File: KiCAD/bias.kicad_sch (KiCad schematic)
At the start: 52 parts, among them Q2 2N7000, Q3 2N7000, U10 OPA454, U11 LM4040LP-5, U12 LM393, U13 OPA1641, U14 OPA1641, U5 OPA454, U9 LM7805_TO220

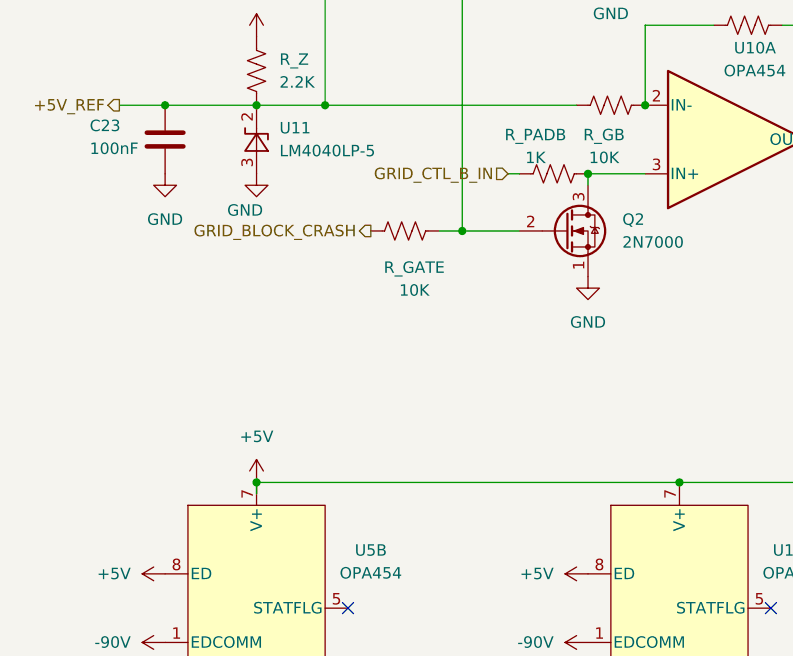
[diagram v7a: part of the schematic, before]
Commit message: front-panel: QT encoder swap, PCF8575 breakout, pre-fab checklist, INT-none decision
Switch STEP + FUNC from direct PCF8575 GPIO to Adafruit I2C QT Rotary
Encoder breakouts (PID 4991) at addr 0x36 / 0x37. The onboard seesaw
SAMD09 handles quadrature decoding + button debounce, dropping ~200
lines of firmware. PCF8575 still covers the LCD (4-bit), paddle, and
panel LEDs.

Add custom KiCad symbols + footprints for both new breakouts to
xmitter.kicad_sym and xmitter.pretty. Footprint properties on the new
symbols are pre-linked, so schematic instances auto-associate. Some
coordinates in both footprints are best-guess pending physical
measurement -- flagged in the descr fields and in the new
front_panel_interface.md open-items subsections.

Decision documented (2026-07-03): no INT wiring back to the Metro.
Firmware polls all three I2C devices at 100 Hz; velocity-adaptive VFO
tuning is computed from delta-position / delta-time in the poll loop.
Rationale and a "here's how to add INT later" path in the new
"Interrupt handling (decision: none)" section of
front_panel_interface.md.

New Documentation/pcb_fab_checklist.md is the consolidated pre-flight
gate before analog-board gerbers ship -- nine sections covering
footprint verification, schematic completeness, ERC/DRC, physical, and
BOM sign-offs. build_checklist.md and CLAUDE.md updated to point at it.

Also in this bundle: SDA/SCL hierarchical labels changed to
bidirectional shape on the VFO, buffer_keyer, and interface sheets
(was an output/input polarity soup that would have failed ERC).
Interface and Front_Panel child sheets registered in .kicad_pro.
Front_Panel is an empty stub; components go in when the sheet is
populated. Adafruit PCF8575 and QT rotary encoder datasheets committed
under Documentation/Components/.

Co-Authored-By: Claude Opus 4.7 <noreply@anthropic.com>
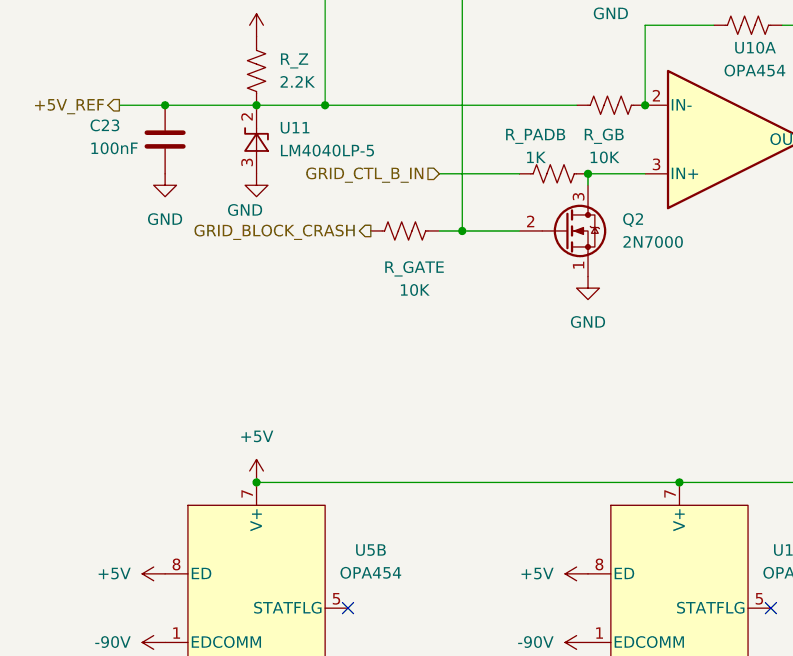
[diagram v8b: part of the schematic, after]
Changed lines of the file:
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@@
 	(wire
 		(pts
-			(xy 67.31 125.73) (xy 66.04 125.73)
+			(xy 67.31 125.73) (xy 58.42 125.73)
 		)
 		(stroke
@@
 		(pts
 			(xy 124.46 173.99) (xy 124.46 181.61)
-		)
-		(stroke
-			(width 0)
-			(type default)
-		)
-	)
-	(wire
-		(pts
-			(xy 38.1 160.02) (xy 38.1 161.29)
 		)
 		(stroke
@@
 	(hierarchical_label "GRID_CTL_B_IN"
 		(shape input)
-		(at 66.04 125.73 180)
+		(at 58.42 125.73 180)
 		(effects
 			(font
